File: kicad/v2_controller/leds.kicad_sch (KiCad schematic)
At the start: 35 parts

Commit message: [kicad] additional work on v2 controller
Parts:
- renumbered C12 to C19, C16 to C20, C20 to C21, C23 to C22, C27 to C23, C13 to C24, C17 to C25, C21 to C26, C24 to C27, C14 to C28, C18 to C29, C22 to C30, C25 to C31, C28 to C32, C15 to C33, C19 to C34, C26 to C35, D36 to D1, D25 to D10, D26 to D11, D27 to D12, D28 to D13, D21 to D14, D22 to D15, D23 to D16, D24 to D17, D37 to D2, D32 to D3, D33 to D4, D34 to D5, D35 to D6, D29 to D7, D30 to D8, D31 to D9, R14 to R18
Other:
- note added: "Key LEDs"

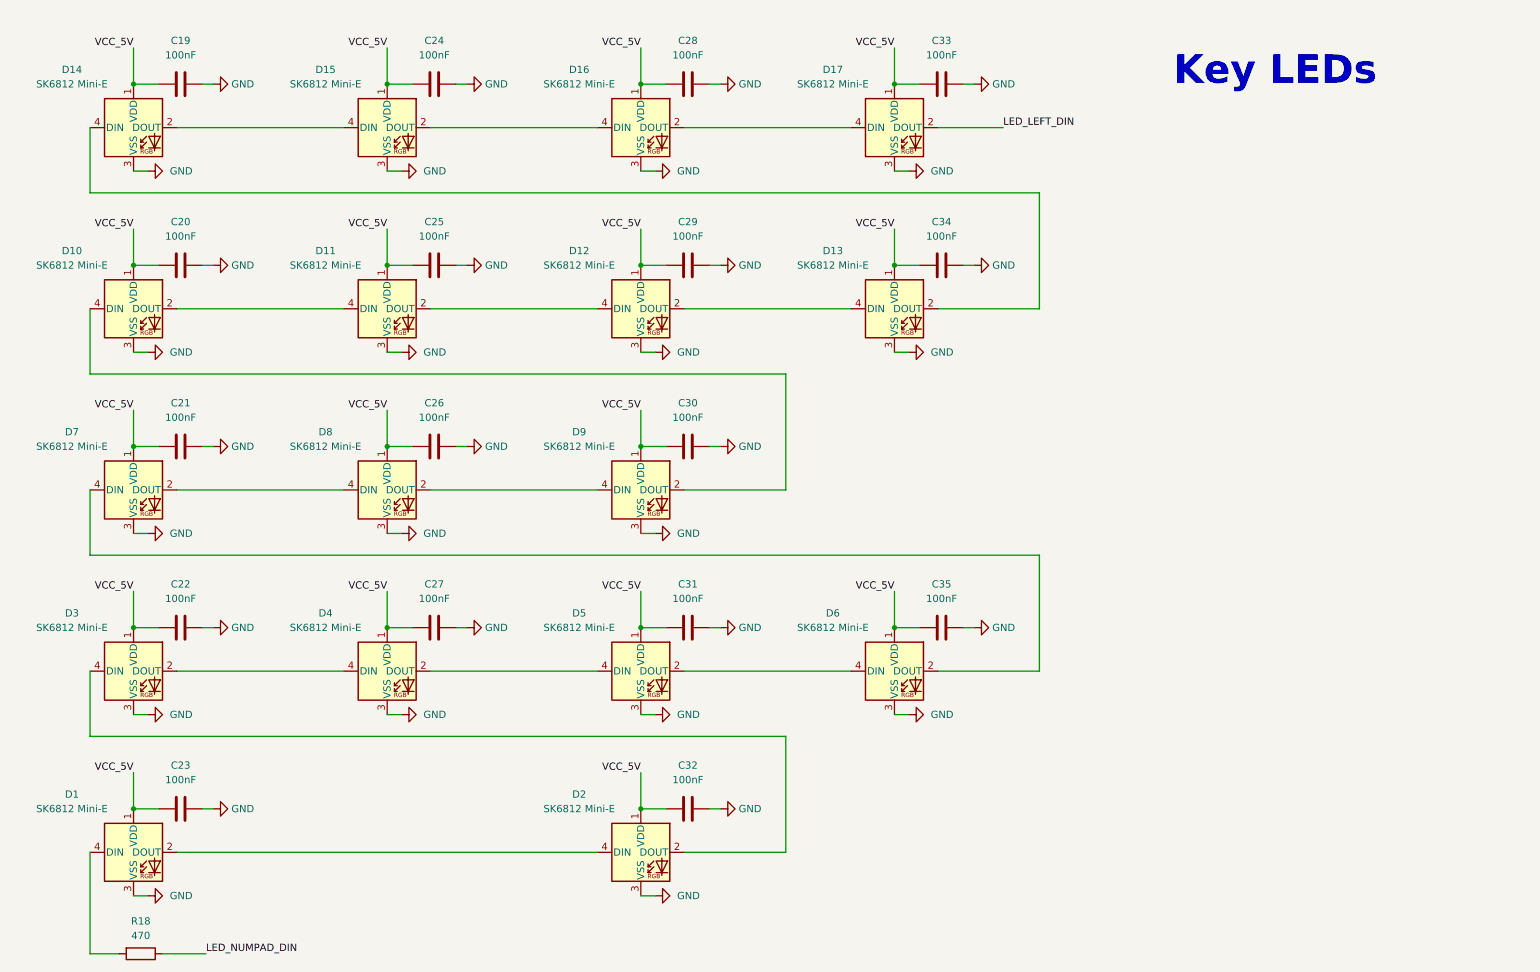
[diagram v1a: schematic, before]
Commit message: [kicad] add status LEDs to the v2 controller
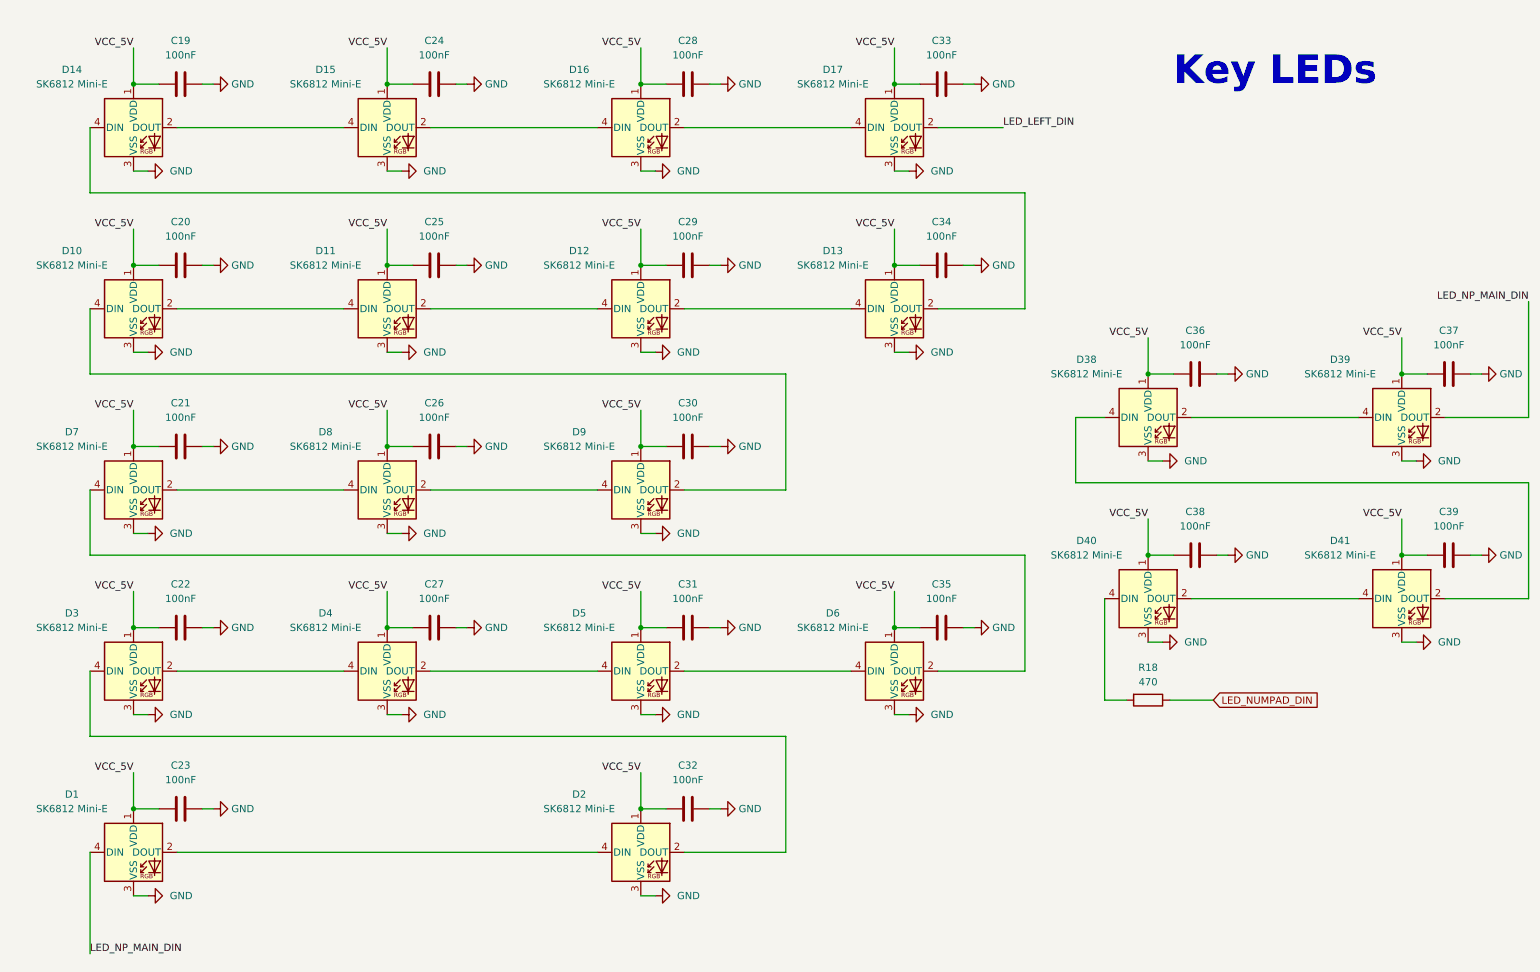
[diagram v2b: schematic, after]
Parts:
- added C36, C37, C38, C39: 100nF, Capacitor_SMD:C_0402_1005Metric, symbol Device:C
- added D38, D39, D40, D41: SK6812 Mini-E, mantyl:SK6812-MINI-E, symbol mantyl:SK6812 Mini-E
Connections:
- net GND: now also C36.1, C37.1, C38.1, C39.1, D38.3 (VSS), D39.3 (VSS), D40.3 (VSS), D41.3 (VSS)
- net VCC_5V: now also C36.2, C37.2, C38.2, C39.2, D38.1 (VDD), D39.1 (VDD), D40.1 (VDD), D41.1 (VDD)
- net at R18.2: now also D40.4 (DIN); no longer D1.4 (DIN)
- new net: D38.2 (DOUT), D39.4 (DIN)
- new net: D40.2 (DOUT), D41.4 (DIN)
- new net: D38.4 (DIN), D41.2 (DOUT)
- new net LED_NP_MAIN_DIN: D1.4 (DIN), D39.2 (DOUT)

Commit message: [kicad] fix global symbol usage in v2 controller
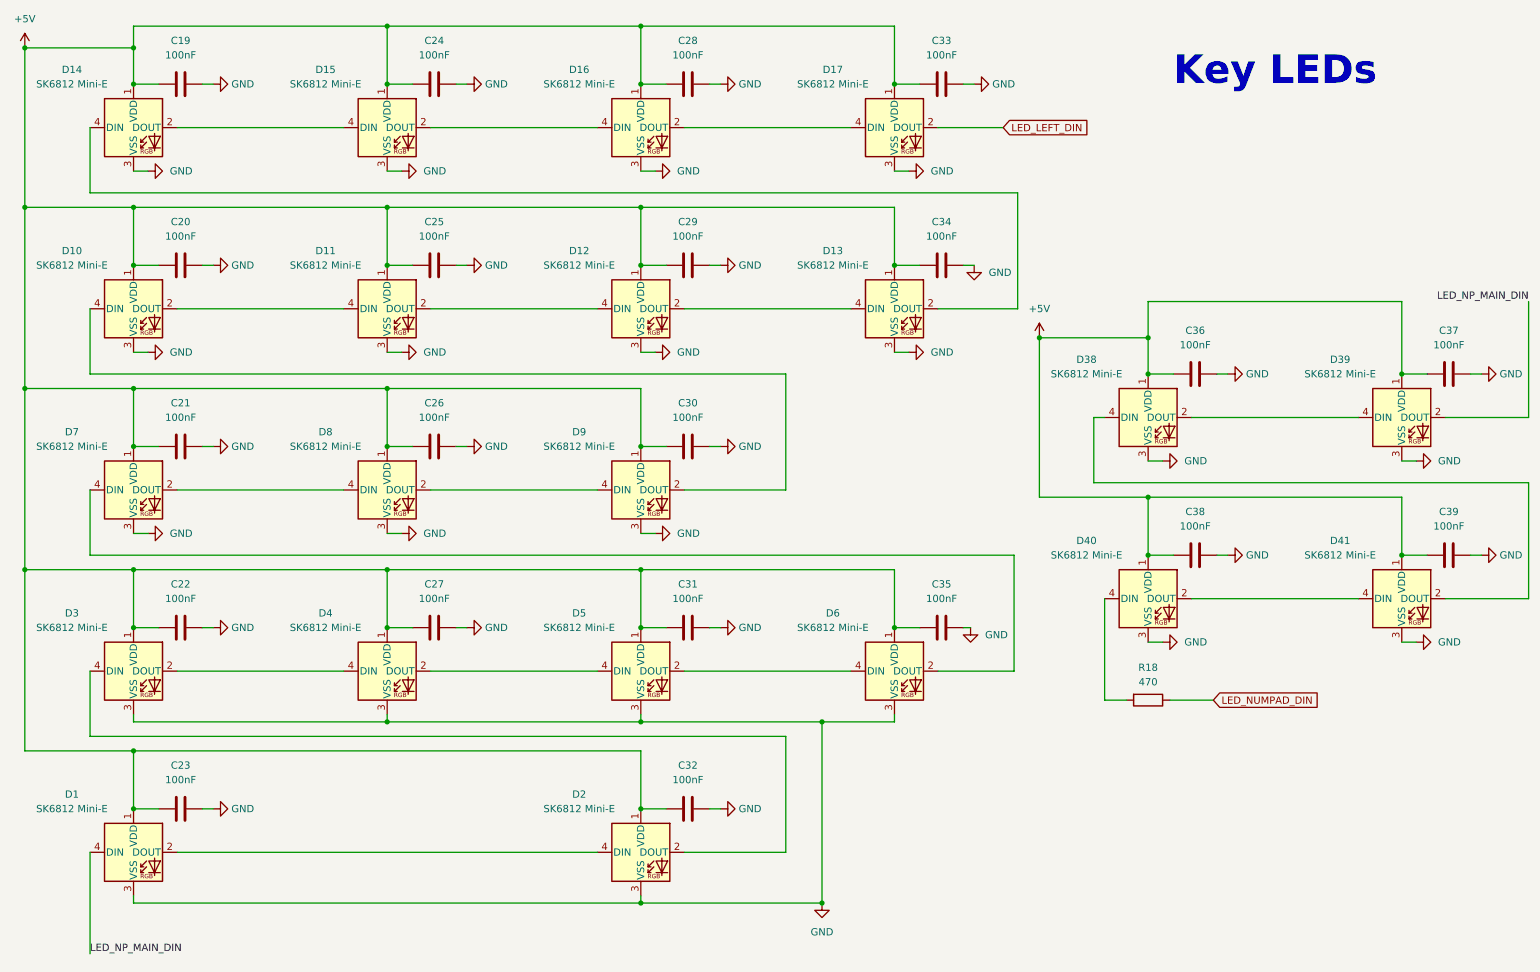
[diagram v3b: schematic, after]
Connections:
- net VCC_5V renamed +5V

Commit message: [kicad] update v2 controller to use hierarchical labels
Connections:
- net LED_LEFT_DIN renamed LED_DOUT
- net LED_NUMPAD_DIN renamed LED_DIN
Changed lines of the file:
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@@
     (effects (font (size 1.27 1.27)) (justify right bottom))
   )
-  (global_label "LED_NUMPAD_DIN" (shape input) (at 227.33 133.35 0) (fields_autoplaced)
+  (hierarchical_label "LED_DOUT" (shape input) (at 190.5 33.02 0) (fields_autoplaced)
     (effects (font (size 1.27 1.27)) (justify left))
-    (property "Intersheetrefs" "${INTERSHEET_REFS}" (at 246.6438 133.35 0)
-      (effects (font (size 1.27 1.27)) (justify left) hide)
-    )
   )
-  (global_label "LED_LEFT_DIN" (shape input) (at 190.5 33.02 0) (fields_autoplaced)
+  (hierarchical_label "LED_DIN" (shape input) (at 227.33 133.35 0) (fields_autoplaced)
     (effects (font (size 1.27 1.27)) (justify left))
-    (property "Intersheetrefs" "${INTERSHEET_REFS}" (at 206.3061 33.02 0)
-      (effects (font (size 1.27 1.27)) (justify left) hide)
-    )
   )
   (symbol (lib_id "power:GND") (at 40.64 104.14 90) (unit 1)

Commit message: [kicad] finish initial component placement
This will probably need to be tweaked further once I begin routing,
but is a start for now.
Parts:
- renumbered R18 to R16
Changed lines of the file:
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@@
   (symbol (lib_id "Device:R") (at 215.9 133.35 270) (unit 1)
     (in_bom yes) (on_board yes) (dnp no) (fields_autoplaced)
-    (property "Reference" "R18" (at 215.9 127.635 90)
+    (property "Reference" "R16" (at 215.9 127 90)
       (effects (font (size 1.27 1.27)))
     )
-    (property "Value" "470" (at 215.9 130.175 90)
+    (property "Value" "470" (at 215.9 129.54 90)
       (effects (font (size 1.27 1.27)))
     )
@@
       (project "v2_controller"
         (path "/102c646f-89e8-474a-be69-05b634400329/58a13171-af4d-4148-bd5d-6db9b6f67a32"
-          (reference "R18") (unit 1)
+          (reference "R16") (unit 1)
         )
       )

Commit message: [kicad] more minor tweaks
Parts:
- renumbered D40 to D38, D41 to D39, D38 to D40, D39 to D41
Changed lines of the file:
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@@
   (symbol (lib_id "mantyl:SK6812 Mini-E") (at 260.35 83.82 0) (unit 1)
     (in_bom yes) (on_board yes) (dnp no)
-    (property "Reference" "D39" (at 249.555 73.66 0)
+    (property "Reference" "D41" (at 249.555 73.66 0)
       (effects (font (size 1.27 1.27)))
     )
@@
       (project "v2_controller"
         (path "/102c646f-89e8-474a-be69-05b634400329/58a13171-af4d-4148-bd5d-6db9b6f67a32"
-          (reference "D39") (unit 1)
+          (reference "D41") (unit 1)
         )
       )
@@
   (symbol (lib_id "mantyl:SK6812 Mini-E") (at 215.9 115.57 0) (unit 1)
     (in_bom yes) (on_board yes) (dnp no)
-    (property "Reference" "D40" (at 205.105 105.41 0)
+    (property "Reference" "D38" (at 205.105 105.41 0)
       (effects (font (size 1.27 1.27)))
     )
@@
       (project "v2_controller"
         (path "/102c646f-89e8-474a-be69-05b634400329/58a13171-af4d-4148-bd5d-6db9b6f67a32"
-          (reference "D40") (unit 1)
+          (reference "D38") (unit 1)
         )
       )
@@
   (symbol (lib_id "mantyl:SK6812 Mini-E") (at 260.35 115.57 0) (unit 1)
     (in_bom yes) (on_board yes) (dnp no)
-    (property "Reference" "D41" (at 249.555 105.41 0)
+    (property "Reference" "D39" (at 249.555 105.41 0)
       (effects (font (size 1.27 1.27)))
     )
@@
       (project "v2_controller"
         (path "/102c646f-89e8-474a-be69-05b634400329/58a13171-af4d-4148-bd5d-6db9b6f67a32"
-          (reference "D41") (unit 1)
+          (reference "D39") (unit 1)
         )
       )
@@
   (symbol (lib_id "mantyl:SK6812 Mini-E") (at 215.9 83.82 0) (unit 1)
     (in_bom yes) (on_board yes) (dnp no)
-    (property "Reference" "D38" (at 205.105 73.66 0)
+    (property "Reference" "D40" (at 205.105 73.66 0)
       (effects (font (size 1.27 1.27)))
     )
@@
       (project "v2_controller"
         (path "/102c646f-89e8-474a-be69-05b634400329/58a13171-af4d-4148-bd5d-6db9b6f67a32"
-          (reference "D38") (unit 1)
-        )
-      )
+          (reference "D40") (unit 1)
+        )
+      )
